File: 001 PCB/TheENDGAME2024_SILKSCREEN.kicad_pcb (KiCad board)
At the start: 2 copper layers, 219 x 96.1 mm, 93 parts, among them J1 B+, J2 B-, SW1 SW_SPDT, SW10 SW_Push, SW11 SW_Push, SW12 SW_Push, SW13 SW_Push, SW14 SW_Push, SW15 SW_Push, SW16 SW_Push, SW17 SW_Push, SW18 SW_Push, SW19 SW_Push, SW2 SW_Push, SW20 SW_Push, SW21 SW_Push, SW22 SW_Push, SW23 SW_Push, SW24 SW_Push, SW25 SW_Push, SW26 SW_Push, SW27 SW_Push, SW28 SW_Push, SW29 SW_Push, SW3 SW_Push, SW30 SW_Push, SW31 SW_Push, SW32 SW_Push, SW33 SW_Push, SW34 SW_Push, SW35 SW_Push, SW36 SW_Push, SW37 SW_Push, SW38 SW_Push, SW4 SW_Push, SW5 SW_Push, SW6 SW_Push, SW7 SW_Push, SW8 SW_Push, SW9 SW_Push, U1 SuperMini nRF52840

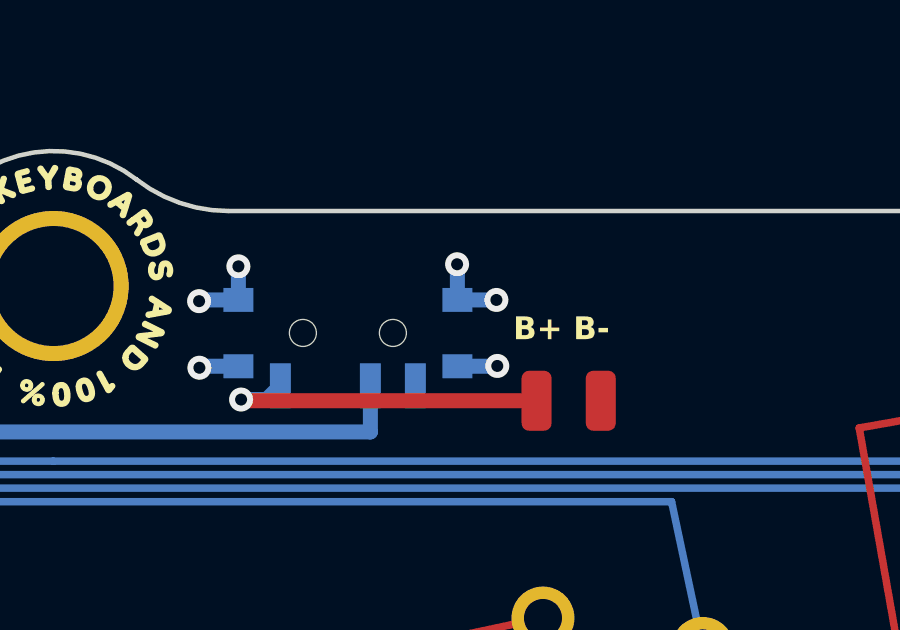
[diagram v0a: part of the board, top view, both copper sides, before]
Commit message: added changed Battery connection pads to JST PicoBlade connector
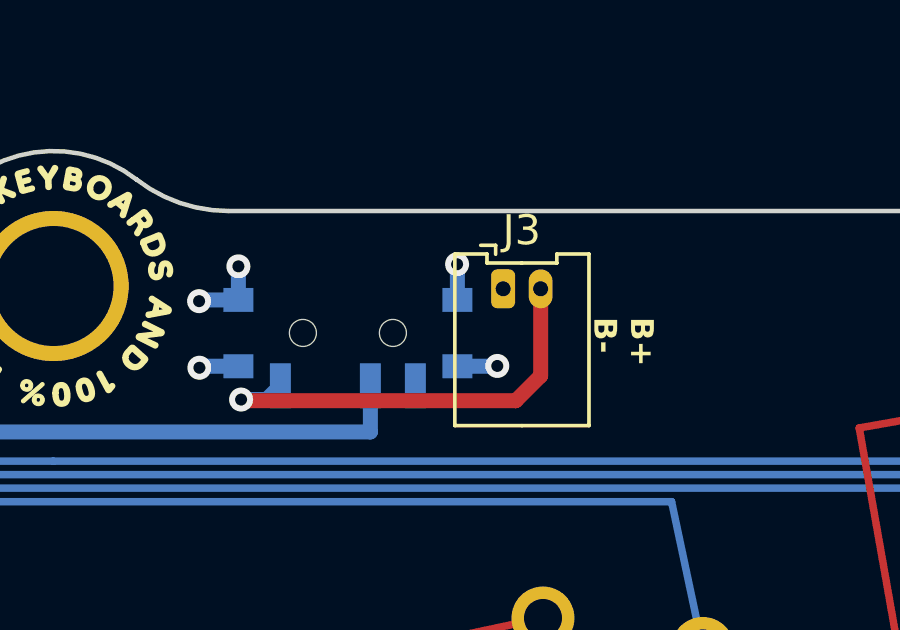
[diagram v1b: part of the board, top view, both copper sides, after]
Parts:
- removed J1: B+, Connector_Wire:SolderWirePad_1x01_SMD_1x2mm
- removed J2: B-, Connector_Wire:SolderWirePad_1x01_SMD_1x2mm
- added J3: Conn_01x02_Pin, Connector_Molex:Molex_PicoBlade_53048-0210_1x02_P1.25mm_Horizontal, F.Cu at (184.9, 68.6)
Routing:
- net Net-(J3-Pin_2): track 10.9 -> 14.7 mm
- net (no net): track 7.60 -> 6.30 mm, vias 6 -> 5
